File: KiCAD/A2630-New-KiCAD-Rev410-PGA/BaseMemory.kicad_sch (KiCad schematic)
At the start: 44 parts, among them SW1 MODE, U300 74HCT05, U400 SDRAM(4Mx16), U401 SDRAM(4Mx16), U606 74HCT244, U800 AP7361C-33ER

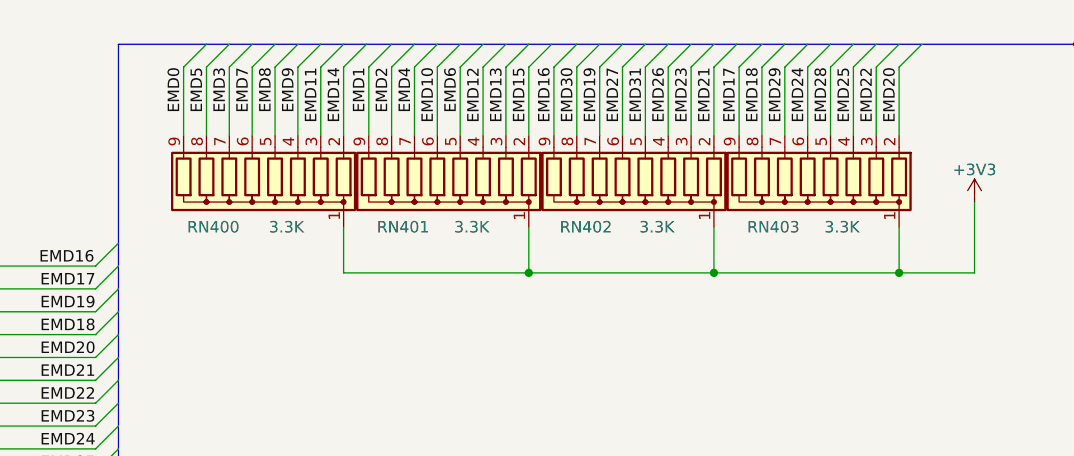
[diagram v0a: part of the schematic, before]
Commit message: Better for SMD assembly now. DRC still not done.
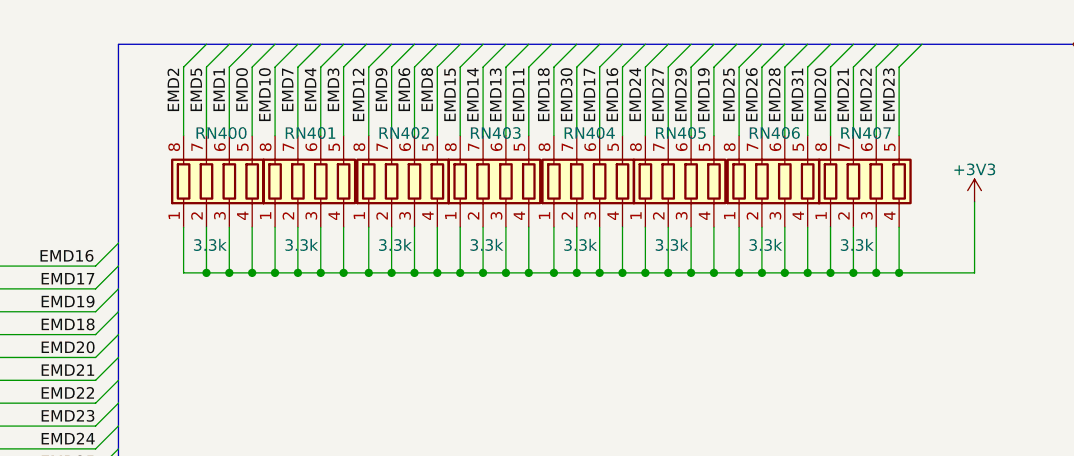
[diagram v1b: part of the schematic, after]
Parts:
- removed RN400, RN401, RN402, RN403: 3.3K, Resistor_THT:R_Array_SIP9, symbol Device:R_Network08
- added RN400, RN401, RN402, RN403, RN404, RN405, RN406, RN407: 3.3k, Resistor_SMD:R_Array_Convex_4x0603, symbol Device:R_Pack04
- C200, C201, C202, C206, C208, C214, C215, C216, C218, C219, C220, C427, C428, C429, C430, C431, C432: LCSC (none) -> C49678
- C205: LCSC (none) -> C1737
- C209: LCSC (none) -> C5378
- C800, C801: LCSC (none) -> C1779
- C802, C804, C805: footprint Capacitor_THT:CP_Radial_D5.0mm_P2.00mm -> Capacitor_SMD:CP_Elec_6.3x5.8; LCSC (none) -> C5246550
- C803: footprint Capacitor_THT:CP_Radial_D5.0mm_P2.00mm -> Capacitor_SMD:CP_Elec_6.3x5.8; LCSC (none) -> C5246536
- R600, R601: LCSC (none) -> C17513
- SW1: LCSC (none) -> C1788496
- U300: LCSC (none) -> C2870691
- U400, U401: LCSC (none) -> C62378
- U606: LCSC (none) -> C6776
- U800: LCSC (none) -> C347222
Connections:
- net +3V3: now also RN400.1 (R1.1), RN400.2 (R2.1), RN400.3 (R3.1), RN400.4 (R4.1), RN401.1 (R1.1), RN401.2 (R2.1), RN401.3 (R3.1), RN401.4 (R4.1), RN402.1 (R1.1), RN402.2 (R2.1), RN402.3 (R3.1), RN402.4 (R4.1), RN403.1 (R1.1), RN403.2 (R2.1), RN403.3 (R3.1), RN403.4 (R4.1), RN404.1 (R1.1), RN404.2 (R2.1), RN404.3 (R3.1), RN404.4 (R4.1), RN405.1 (R1.1), RN405.2 (R2.1), RN405.3 (R3.1), RN405.4 (R4.1), RN406.1 (R1.1), RN406.2 (R2.1), RN406.3 (R3.1), RN406.4 (R4.1), RN407.1 (R1.1), RN407.2 (R2.1), RN407.3 (R3.1), RN407.4 (R4.1)
- net EMD0: now also RN400.5 (R4.2)
- net EMD1: now also RN400.6 (R3.2)
- net EMD10: now also RN401.8 (R1.2)
- net EMD11: now also RN403.5 (R4.2)
- net EMD12: now also RN402.8 (R1.2)
- net EMD13: now also RN403.6 (R3.2)
- net EMD14: now also RN403.7 (R2.2)
- net EMD15: now also RN403.8 (R1.2)
- net EMD16: now also RN404.5 (R4.2)
- net EMD17: now also RN404.6 (R3.2)
- net EMD18: now also RN404.8 (R1.2)
- net EMD19: now also RN405.5 (R4.2)
- net EMD2: now also RN400.8 (R1.2)
- net EMD20: now also RN407.8 (R1.2)
- net EMD21: now also RN407.7 (R2.2)
- net EMD22: now also RN407.6 (R3.2)
- net EMD23: now also RN407.5 (R4.2)
- net EMD24: now also RN405.8 (R1.2)
- net EMD25: now also RN406.8 (R1.2)
- net EMD26: now also RN406.7 (R2.2)
- net EMD27: now also RN405.7 (R2.2)
- net EMD28: now also RN406.6 (R3.2)
- net EMD29: now also RN405.6 (R3.2)
- net EMD3: now also RN401.5 (R4.2)
- net EMD30: now also RN404.7 (R2.2)
- net EMD31: now also RN406.5 (R4.2)
- net EMD4: now also RN401.6 (R3.2)
- net EMD5: now also RN400.7 (R2.2)
- net EMD6: now also RN402.6 (R3.2)
- net EMD7: now also RN401.7 (R2.2)
- net EMD8: now also RN402.5 (R4.2)
- net EMD9: now also RN402.7 (R2.2)
